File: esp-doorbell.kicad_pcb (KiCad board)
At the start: 2 copper layers, 0 parts

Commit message: fix schematics, add layout
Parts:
- added C1: 1uF, Capacitor_SMD:C_0402_1005Metric, F.Cu at (100.5, 118.0)
- added C2: 1000uF, Capacitor_SMD:CP_Elec_10x12.5, F.Cu at (77.0, 90.1)
- added C3: 1000uF, Capacitor_SMD:CP_Elec_10x12.5, F.Cu at (77.0, 101.1)
- added C4: 1000uF, Capacitor_SMD:CP_Elec_10x12.5, F.Cu at (77.0, 112.1)
- added C5: 10nF, Capacitor_SMD:C_0402_1005Metric, F.Cu at (83.5, 98.0)
- added C6: 220uF, Capacitor_SMD:CP_Elec_6.3x7.7, F.Cu at (88.9, 111.5)
- added C7: 1uF, Capacitor_SMD:C_0402_1005Metric, F.Cu at (99.5, 138.5)
- added D1: RMB2S, Package_TO_SOT_SMD:TO-269AA, F.Cu at (89.4, 87.2)
- added D2: Red LED, LED_SMD:LED_0603_1608Metric, F.Cu at (101.7, 73.5)
- added D3: SM4007PL, Diode_SMD:D_SOD-123F, F.Cu at (73.9, 75.0)
- added D4: D, Diode_SMD:D_SMA, F.Cu at (89.1, 91.8)
- added D5: Red LED, LED_SMD:LED_0603_1608Metric, F.Cu at (101.7, 75.5)
- added D6: Red LED, LED_SMD:LED_0603_1608Metric, F.Cu at (101.7, 77.5)
- added F1: Fuse, LED_SMD:LED_1206_3216Metric, F.Cu at (84.9, 94.9)
- added H1: MountingHole_Pad, MountingHole:MountingHole_3.2mm_M3_DIN965_Pad, F.Cu at (73.0, 69.5)
- added H2: MountingHole_Pad, MountingHole:MountingHole_3.2mm_M3_DIN965_Pad, F.Cu at (100.0, 69.5)
- added H3: MountingHole_Pad, MountingHole:MountingHole_3.2mm_M3_DIN965_Pad, F.Cu at (73.0, 136.0)
- added J1: Screw_Terminal_01x02, TerminalBlock_Phoenix:TerminalBlock_Phoenix_MKDS-1,5-2-5.08_1x02_P5.08mm_Horizontal, F.Cu at (77.6, 60.5)
- added J2: Screw_Terminal_01x02, TerminalBlock_Phoenix:TerminalBlock_Phoenix_MKDS-1,5-2-5.08_1x02_P5.08mm_Horizontal, F.Cu at (89.0, 60.5)
- added J3: Screw_Terminal_01x02, TerminalBlock_Phoenix:TerminalBlock_Phoenix_MKDS-1,5-2-5.08_1x02_P5.08mm_Horizontal, F.Cu at (100.6, 60.5)
- added K1: JQC-3FF-005-1Z, Relay_THT:Relay_SPDT_Hongfa_JQC-3FF_0XX-1Z, F.Cu at (92.2, 80.5)
- added L1: 15uH, Inductor_SMD:L_Changjiang_FNR5040S, F.Cu at (87.0, 104.9)
- added Q1: NMOS, Package_TO_SOT_SMD:SOT-23-3, F.Cu at (74.3, 81.4)
- added R1: 10K, Resistor_SMD:R_0603_1608Metric, F.Cu at (99.9, 116.5)
- added R2: 100R, Resistor_SMD:R_0603_1608Metric, F.Cu at (98.5, 79.5)
- added R3: 470R, Resistor_SMD:R_0603_1608Metric, F.Cu at (98.5, 73.5)
- added R4: 200R, Resistor_SMD:R_0603_1608Metric, F.Cu at (74.7, 78.5)
- added R5: 10K, Resistor_SMD:R_0603_1608Metric, F.Cu at (74.7, 77.0)
- added R6: 10K, Resistor_SMD:R_0603_1608Metric, F.Cu at (91.6, 104.8)
- added R7: 3.3K, Resistor_SMD:R_0603_1608Metric, F.Cu at (91.6, 106.3)
- added R8: 200R, Resistor_SMD:R_0603_1608Metric, F.Cu at (98.5, 75.5)
- added R9: 200R, Resistor_SMD:R_0603_1608Metric, F.Cu at (98.5, 77.5)
- added TP1: Rectifier, TestPoint:TestPoint_Pad_D1.0mm, F.Cu at (88.5, 95.0)
- added TP2: 5V, TestPoint:TestPoint_Pad_D1.0mm, F.Cu at (90.0, 116.5)
- added U1: TPS5430DDA, Package_SO:TI_SO-PowerPAD-8_ThermalVias, F.Cu at (88.8, 99.1)
- added U2: XIAO-ESP32-S3-SMD, Seeed Studio XIAO Series Library:XIAO-ESP32C6-SMD, F.Cu at (92.9, 128.6)
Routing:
- net GND: track 0.00 -> 105.2 mm, vias 0 -> 15
- net AC1: track 0.00 -> 83.9 mm
- net D0: track 0.00 -> 73.0 mm, vias 0 -> 1
- net +3V3: track 0.00 -> 69.9 mm, vias 0 -> 2
- net +5V: track 0.00 -> 65.1 mm, vias 0 -> 3
- net D1: track 0.00 -> 62.4 mm, vias 0 -> 2
- net AC2: track 0.00 -> 49.8 mm
- net D2: track 0.00 -> 48.9 mm, vias 0 -> 2
- net Net-(D2-K): track 0.00 -> 45.8 mm, vias 0 -> 1
- net Net-(D1-+): track 0.00 -> 38.2 mm
- net Net-(J2-Pin_2): track 0.00 -> 35.3 mm, vias 0 -> 1
- net Net-(D4-K): track 0.00 -> 27.9 mm
- net Net-(J3-Pin_1): track 0.00 -> 16.6 mm
- net Net-(U1-VSENSE): track 0.00 -> 10.9 mm
- net Net-(U1-VIN): track 0.00 -> 8.58 mm
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- added copper zone on F.Cu, net +5V
- added copper zone on B.Cu, net GND
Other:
- board outline added: 34 x 84 mm

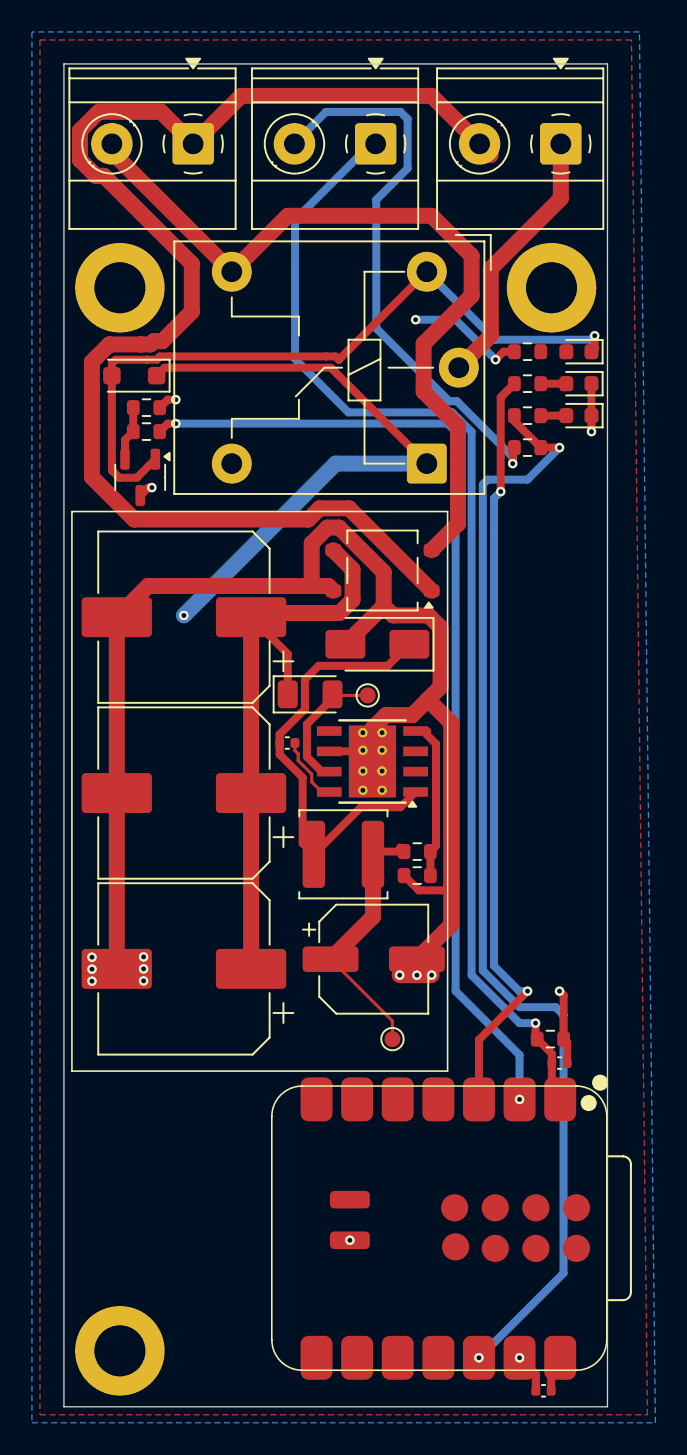
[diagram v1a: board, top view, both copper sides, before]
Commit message: make board a bit smaller
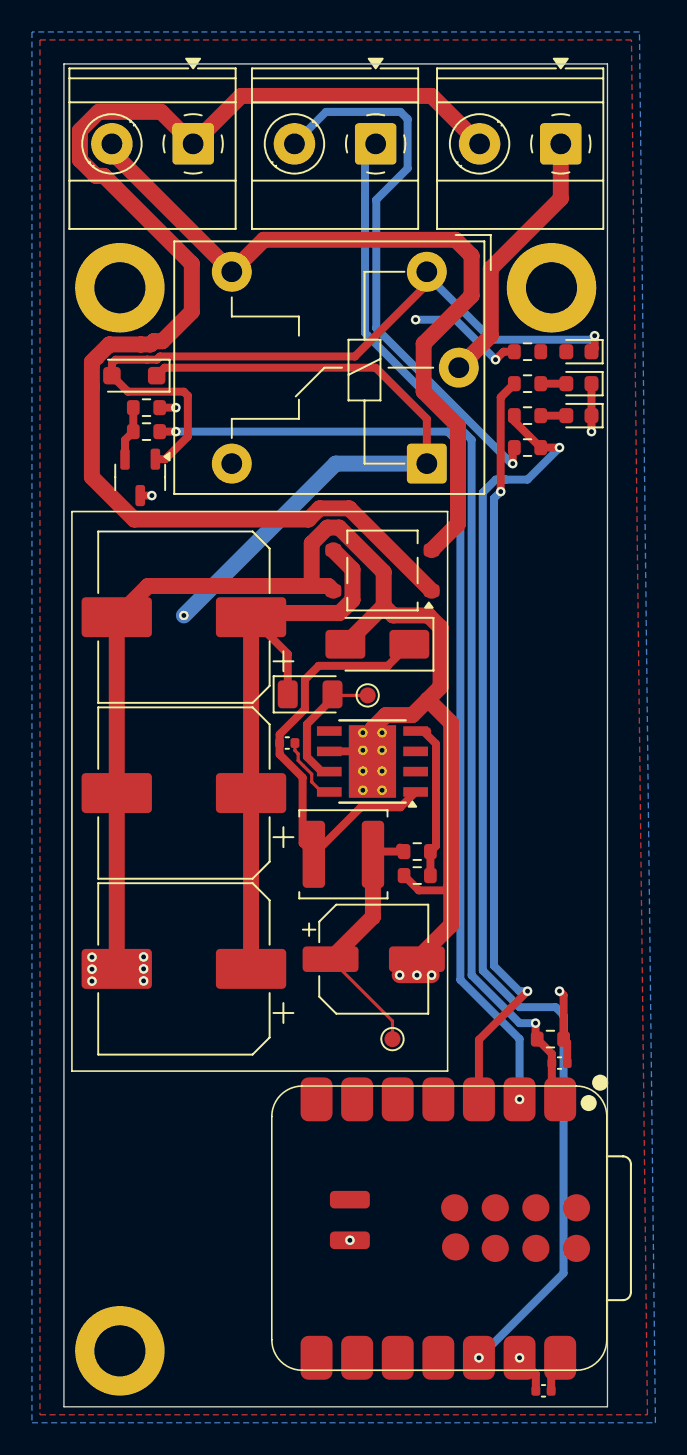
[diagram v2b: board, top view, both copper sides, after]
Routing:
- net D0: track 73.0 -> 67.8 mm
- net +5V: track 65.1 -> 66.7 mm
- net Net-(D2-K): track 45.8 -> 47.3 mm
- net AC2: track 49.8 -> 48.6 mm
- net AC1: track 83.9 -> 82.9 mm
- net D1: track 62.4 -> 61.6 mm

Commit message: save changes
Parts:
- moved C7 21.9 mm to (80.4, 127.7), turned to 90 degrees
- moved R7 19.8 mm to (99.8, 88.3), turned to 90 degrees
- moved C4 17.3 mm to (89.8, 100.5)
- moved C5 17.0 mm to (93.8, 84.4)
- moved R6 15.4 mm to (99.8, 91.8), turned to -90 degrees
- moved TP1 15.2 mm to (99.3, 84.3)
- moved L1 15.1 mm to (99.3, 96.3)
- moved C6 12.4 mm to (99.5, 105.0), turned to -90 degrees
- moved U1 12.0 mm to (96.0, 89.5), turned to 90 degrees
- moved R1 11.9 mm to (102.4, 128.1), turned to -90 degrees
- moved C1 10.7 mm to (100.9, 128.7), turned to -90 degrees
- moved TP2 9.64 mm to (93.5, 107.5)
- moved H3 8.00 mm to (73.0, 128.0)
- moved U2 7.88 mm to (90.4, 121.1), turned to 180 degrees
- moved D4 4.61 mm to (90.8, 87.5), turned to -90 degrees
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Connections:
- U2 pad 16: GND -> unconnected-(U2-GND-Pad16)
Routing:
- net AC1: track 82.9 -> 50.1 mm
- net AC2: track 48.6 -> 29.3 mm
- net Net-(U1-VIN): track 8.58 -> 23.8 mm
- net +5V: track 66.7 -> 52.5 mm
- net D0: track 67.8 -> 80.0 mm
- net Net-(D4-K): track 27.9 -> 17.4 mm
- net D1: track 61.6 -> 71.0 mm
- net Net-(D2-K): track 47.3 -> 55.2 mm
- net D2: track 48.9 -> 54.5 mm
- net Net-(D1-+): track 38.2 -> 33.8 mm
- net Net-(U1-VSENSE): track 10.9 -> 6.95 mm
- net GND: track 104.8 -> 102.8 mm, vias 15 -> 8
- net Net-(U1-PH): track 4.23 -> 2.42 mm
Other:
- board size 34 x 84 mm -> 34 x 78 mm

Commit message: cleanup, add silkscreen
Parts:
- moved TP1 2.09 mm to (101.0, 85.5)
- moved L1 1.16 mm to (98.2, 96.1)
- turned C4 to 0 degrees
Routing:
- net GND: track 102.8 -> 10.1 mm, vias 8 -> 0
- net +5V: track 52.5 -> 30.9 mm, vias 3 -> 6
- net Net-(D1-+): track 33.8 -> 21.6 mm
- net +3V3: track 69.1 -> 71.3 mm
- net Net-(U1-VIN): track 23.8 -> 26.0 mm
- net Net-(D2-A): track 0.00 -> 1.60 mm
- net Net-(D4-K): track 17.4 -> 16.0 mm
- net D1: track 71.0 -> 70.3 mm
- net D0: track 80.0 -> 79.4 mm
- net D2: track 54.5 -> 54.4 mm, vias 2 -> 3
- added copper zone on B.Cu, net +5V
- added copper zone on F.Cu, net GND
- removed copper zone on F.Cu, net +5V
- removed copper zone on B.Cu, net GND
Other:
- board size 34 x 78 mm -> 34 x 76 mm
- board text added: "AC-DC"
- board text added: "Button"
- board text added: "Chime"
- board text added: "Chime User MCU"
- board text added: "Doorbell zigbee connector By Mees V1.0"
- board text added: "Seeed Studio Xiao C6"
- board text added: "Transformer"
